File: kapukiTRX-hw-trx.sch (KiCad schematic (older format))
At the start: 33 parts, among them J1 GPS, J2 SWD, J21 Conn_01x01, J22 Conn_01x01, U1 STM32G474VE, U2 LP38693-3.3, Y1 16MHz

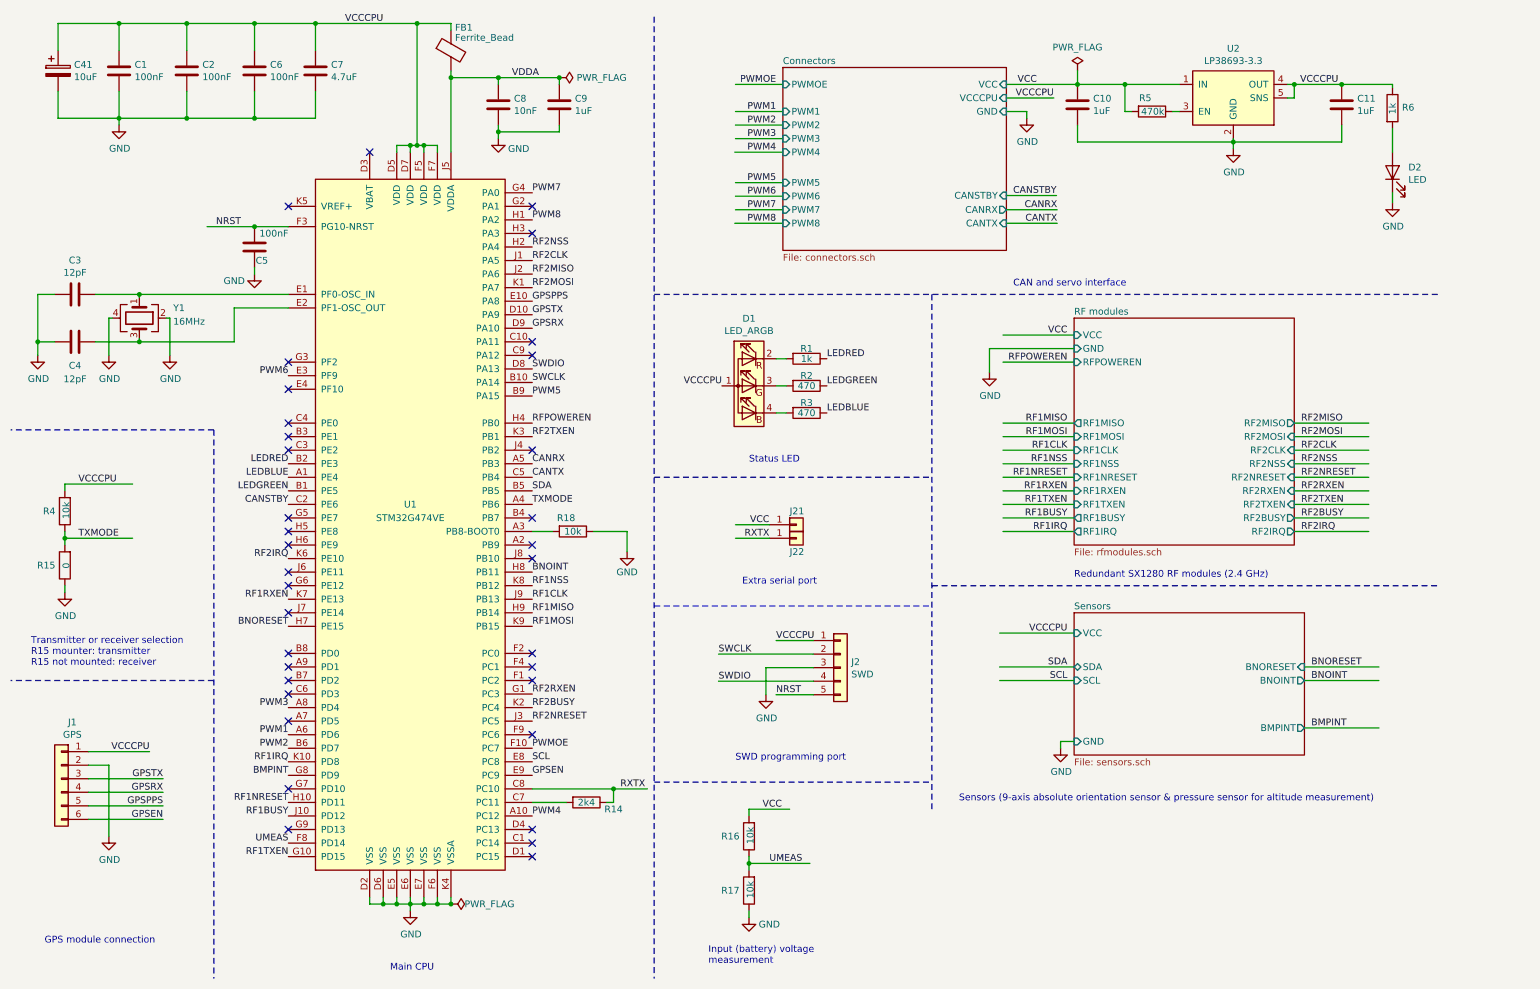
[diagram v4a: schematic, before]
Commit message: Add pull-up for uart
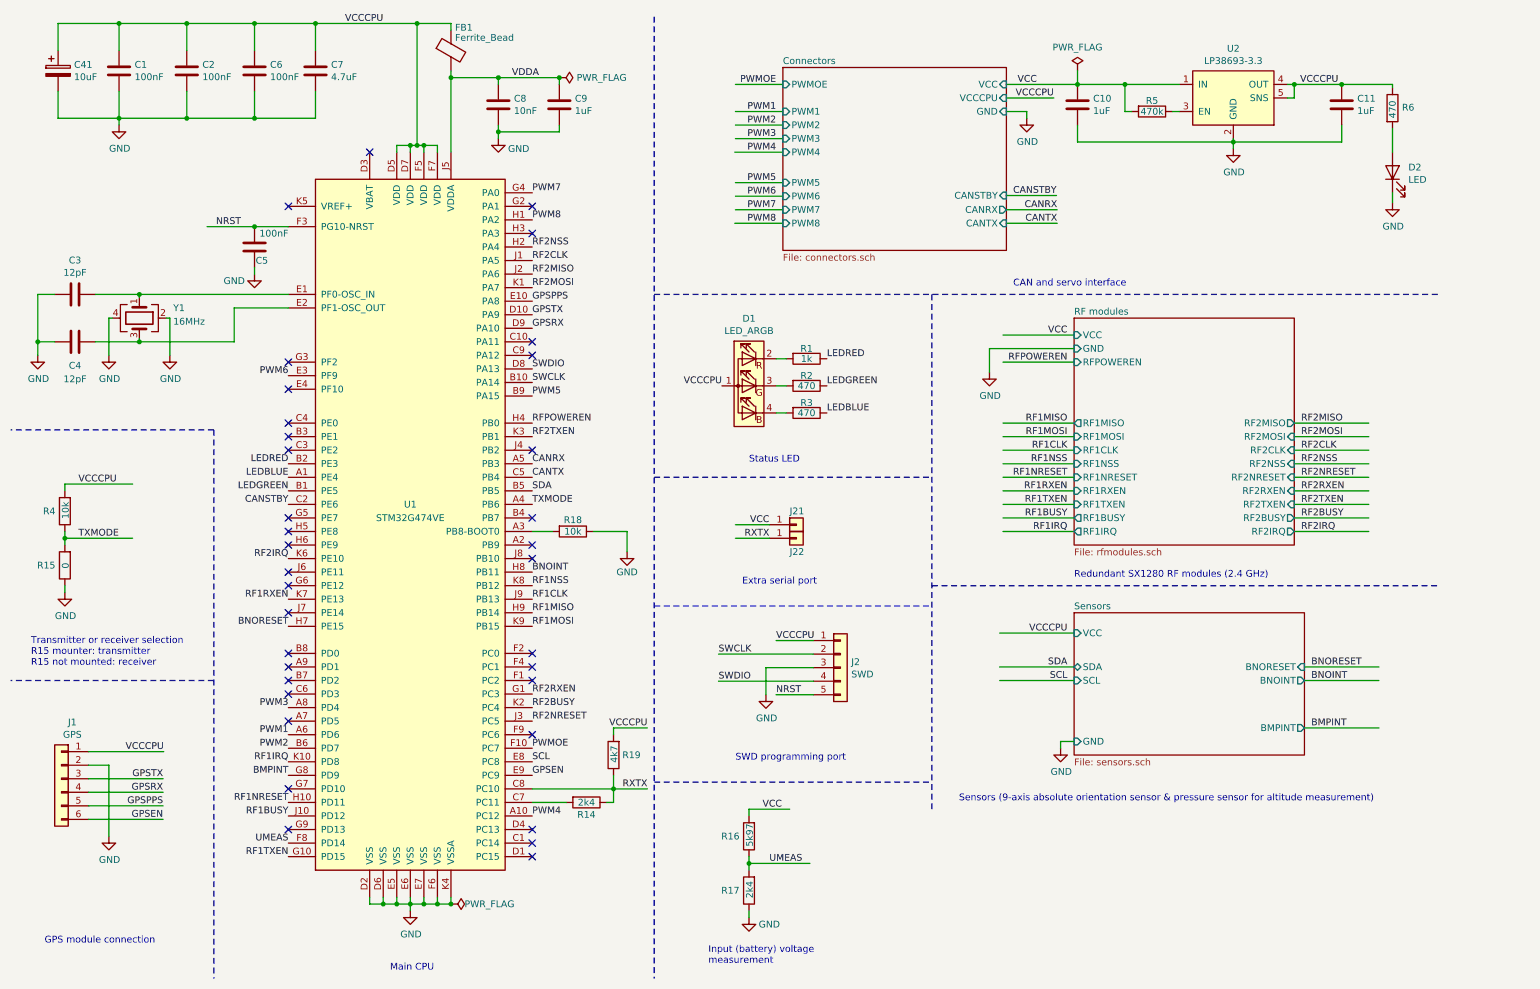
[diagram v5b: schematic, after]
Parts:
- added R19: 4k7, Resistor_SMD:R_0402_1005Metric, symbol Device:R
- R16: value 10k -> 5k97
- R17: value 10k -> 2k4
- R6: value 1k -> 470
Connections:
- wire segments 178 -> 181
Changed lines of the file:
@@
 U 1 1 5C8015BC
 P 9025 1300
-F 0 "R5" V 8925 1250 50  0000 C CNN
-F 1 "470k" V 9025 1305 50  0000 C CNN
+F 0 "R5" V 8945 1300 50  0000 C CNN
+F 1 "470k" V 9025 1300 50  0000 C CNN
 F 2 "Resistor_SMD:R_0402_1005Metric" V 8955 1300 50  0001 C CNN
 F 3 "~" H 9025 1300 50  0001 C CNN
@@
 P 10800 1275
 F 0 "R6" H 10870 1280 50  0000 L CNN
-F 1 "1k" V 10800 1230 50  0000 L CNN
+F 1 "470" V 10800 1200 50  0000 L CNN
 F 2 "Resistor_SMD:R_0402_1005Metric" V 10730 1275 50  0001 C CNN
 F 3 "~" H 10800 1275 50  0001 C CNN
@@
 Text Label 1725 6325 2    50   ~ 0
 GPSRX
-Text Label 1625 6025 2    50   ~ 0
+Text Label 1730 6025 2    50   ~ 0
 VCCCPU
 Wire Wire Line
-	1175 6025 1625 6025
+	1175 6025 1730 6025
 Wire Wire Line
 	1325 6125 1175 6125
@@
 P 1000 4250
 F 0 "R4" H 1070 4250 50  0000 L CNN
-F 1 "10k" V 990 4180 50  0000 L CNN
+F 1 "10k" V 995 4180 50  0000 L CNN
 F 2 "Resistor_SMD:R_0402_1005Metric" V 930 4250 50  0001 C CNN
 F 3 "~" H 1000 4250 50  0001 C CNN
@@
 U 1 1 5DC9D66B
 P 4850 6400
-F 0 "R14" V 4900 6600 50  0000 C CNN
+F 0 "R14" V 4940 6400 50  0000 C CNN
 F 1 "2k4" V 4850 6400 50  0000 C CNN
 F 2 "Resistor_SMD:R_0402_1005Metric" V 4780 6400 50  0001 C CNN
@@
 Wire Wire Line
 	5050 6400 5050 6300
-Text Label 5100 6300 0    50   ~ 0
+Text Label 5300 6300 2    50   ~ 0
 RXTX
 Wire Wire Line
@@
 P 1000 4650
 F 0 "R15" H 1070 4650 50  0000 L CNN
-F 1 "0" V 990 4630 50  0000 L CNN
+F 1 "0" V 995 4630 50  0000 L CNN
 F 2 "Resistor_SMD:R_0402_1005Metric" V 930 4650 50  0001 C CNN
 F 3 "~" H 1000 4650 50  0001 C CNN
@@
 P 6050 6650
 F 0 "R16" H 6120 6650 50  0000 L CNN
-F 1 "10k" V 6040 6580 50  0000 L CNN
+F 1 "5k97" V 6045 6555 50  0000 L CNN
 F 2 "Resistor_SMD:R_0402_1005Metric" V 5980 6650 50  0001 C CNN
 F 3 "~" H 6050 6650 50  0001 C CNN
@@
 P 6050 7050
 F 0 "R17" H 6120 7050 50  0000 L CNN
-F 1 "10k" V 6040 6980 50  0000 L CNN
+F 1 "2k4" V 6045 6980 50  0000 L CNN
 F 2 "Resistor_SMD:R_0402_1005Metric" V 5980 7050 50  0001 C CNN
 F 3 "~" H 6050 7050 50  0001 C CNN
@@
 U 1 1 5E907618
 P 4750 4400
-F 0 "R18" V 4650 4350 50  0000 C CNN
+F 0 "R18" V 4665 4400 50  0000 C CNN
 F 1 "10k" V 4750 4400 50  0000 C CNN
 F 2 "Resistor_SMD:R_0402_1005Metric" V 4680 4400 50  0001 C CNN
@@
 	5150 4400 5150 4550
 NoConn ~ 4450 4500
+$Comp
+L Device:R R19
+U 1 1 5E99423B
+P 5050 6050
+F 0 "R19" H 4850 6050 50  0000 L CNN
+F 1 "4k7" V 5045 5980 50  0000 L CNN
+F 2 "Resistor_SMD:R_0402_1005Metric" V 4980 6050 50  0001 C CNN
+F 3 "~" H 5050 6050 50  0001 C CNN
+	1    5050 6050
+	-1   0    0    1
+$EndComp
+Wire Wire Line
+	5050 6300 5050 6200
+Wire Wire Line
+	5050 5900 5050 5850
+Wire Wire Line
+	5050 5850 5300 5850
+Text Label 5300 5850 2    50   ~ 0
+VCCCPU
 $EndSCHEMATC

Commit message: Make some value changes for consistency
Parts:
- R16: value 5k97 -> 5k97 0.1%
- R17: value 2k4 -> 2k4 0.1%
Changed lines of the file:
@@
 EESchema Schematic File Version 4
-LIBS:kapukiTRX-hw-trx-cache
 EELAYER 30 0
 EELAYER END
@@
 P 6050 6650
 F 0 "R16" H 6120 6650 50  0000 L CNN
-F 1 "5k97" V 6045 6555 50  0000 L CNN
+F 1 "5k97 0.1%" H 6110 6750 50  0000 L CNN
 F 2 "Resistor_SMD:R_0402_1005Metric" V 5980 6650 50  0001 C CNN
 F 3 "~" H 6050 6650 50  0001 C CNN
@@
 P 6050 7050
 F 0 "R17" H 6120 7050 50  0000 L CNN
-F 1 "2k4" V 6045 6980 50  0000 L CNN
+F 1 "2k4 0.1%" H 6110 7130 50  0000 L CNN
 F 2 "Resistor_SMD:R_0402_1005Metric" V 5980 7050 50  0001 C CNN
 F 3 "~" H 6050 7050 50  0001 C CNN
